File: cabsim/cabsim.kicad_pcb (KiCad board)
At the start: 2 copper layers, 87 x 30 mm, 45 parts, among them J1 NJ3FD-V, J3 Conn_01x01, J4 Conn_01x01, J5 NJ3FD-V, U3 Op_Amp_Dual, U4 Opamp_Quad

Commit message: update pcb
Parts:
- C4: value 1n -> 3.3n
- C7: value 2.2n -> 3.3n
- R19: value 390 -> 330
- R5, R9: value 3.9k -> 3.3k
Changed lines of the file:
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@@
 			)
 		)
-		(property "Value" "390"
+		(property "Value" "330"
 			(at 3.81 2.31 90)
 			(layer "F.Fab")
@@
 			)
 		)
-		(property "Value" "3.9k"
+		(property "Value" "3.3k"
 			(at 3.81 2.31 90)
 			(layer "F.Fab")
@@
 			)
 		)
-		(property "Value" "3.9k"
+		(property "Value" "3.3k"
 			(at 3.81 2.31 90)
 			(layer "F.Fab")
@@
 			)
 		)
-		(property "Value" "2.2n"
+		(property "Value" "3.3n"
 			(at 2.5 -2.31 90)
 			(layer "B.Fab")
@@
 			)
 		)
-		(property "Value" "1n"
+		(property "Value" "3.3n"
 			(at 2.5 -2.31 90)
 			(layer "B.Fab")

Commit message: update pcb and gitignore
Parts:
- C10, C12, C2, C9: moved to F.Cu
- moved R1 29.2 mm to (111.5, 83.3), turned to 180 degrees
- moved C2 27.3 mm to (108.7, 88.6)
- moved R17 27.0 mm to (152.5, 97.7), turned to 0 degrees
- moved R19 26.3 mm to (141.1, 81.4), turned to 0 degrees
- moved R5 20.8 mm to (115.8, 94.7)
- moved C12 19.2 mm to (115.7, 97.4)
- moved J3 19.0 mm to (98.8, 72.1)
- moved J4 18.6 mm to (116.2, 72.0)
- moved C14 18.4 mm to (147.0, 84.8), turned to 0 degrees
- moved R8 17.4 mm to (133.2, 94.9)
- moved R9 17.4 mm to (136.4, 87.2)
- moved C6 17.1 mm to (133.3, 97.5)
- moved C13 16.4 mm to (141.6, 84.8)
- moved R6 14.2 mm to (119.2, 87.0)
- moved C15 13.3 mm to (164.5, 87.7), turned to -90 degrees
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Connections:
- C2 pad 1: Net-(U4A-+) -> Net-(U4D-+)
- C4 pad 2: Net-(U4A--) -> Net-(U4D--)
- C5 pad 1: Net-(U4D-+) -> Net-(U4A-+)
- C7 pad 2: Net-(U4D--) -> Net-(U4A--)
- R1 pad 1: Net-(U4A-+) -> Net-(U4D-+)
- R5 pad 2: Net-(U4A--) -> Net-(U4D--)
- R6 pad 1: Net-(U4A--) -> Net-(U4D--)
- R8 pad 2: Net-(U4D-+) -> Net-(U4A-+)
- R9 pad 1: Net-(U4D--) -> Net-(U4A--)
- RV1 pad 1: Net-(U4D--) -> Net-(U4A--)
- RV1 pad 2: Net-(U4D--) -> Net-(U4A--)
- U4 pad 1: Net-(C4-Pad1) -> Net-(C7-Pad1)
- U4 pad 14: Net-(C7-Pad1) -> Net-(C4-Pad1)
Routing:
- net Net-(U4A--): track 10.4 -> 52.1 mm
- net Net-(U4D--): track 48.0 -> 9.47 mm
- net Net-(C2-Pad2): track 27.3 -> 5.31 mm
- net Net-(C15-Pad2): track 15.4 -> 37.1 mm
- net Net-(C10-Pad1): track 51.9 -> 64.2 mm
- net Net-(U3A-+): track 23.7 -> 35.6 mm
- net Net-(U3B-+): track 17.5 -> 7.97 mm
- net GND: track 14.5 -> 5.25 mm
- net /vref: track 110.4 -> 101.2 mm
- net Net-(U4D-+): track 9.69 -> 18.7 mm
- net Net-(U3C-V+): track 76.3 -> 84.4 mm
- net Net-(C13-Pad1): track 25.2 -> 17.1 mm
- net Net-(C7-Pad1): track 9.52 -> 16.9 mm
- net Net-(D1-A): track 20.1 -> 12.8 mm
- net Net-(U4A-+): track 12.5 -> 6.39 mm
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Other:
- outline, holes or cut-outs redrawn

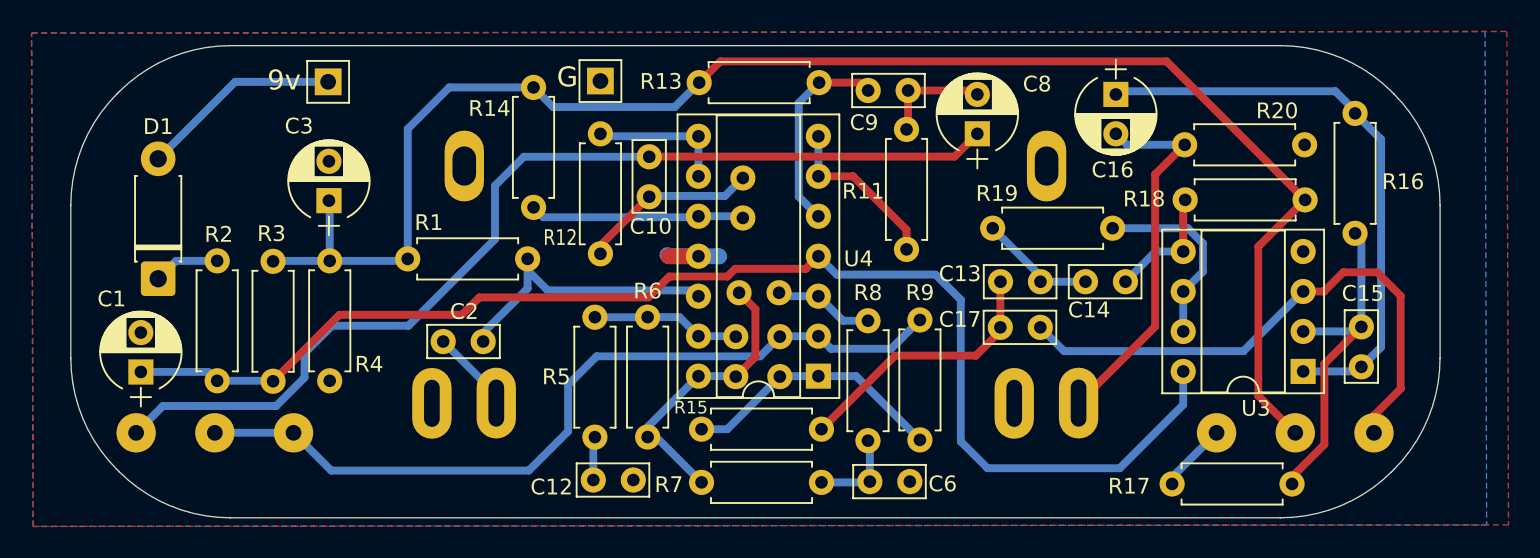
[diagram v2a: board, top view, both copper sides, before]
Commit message: minor routing adjustments
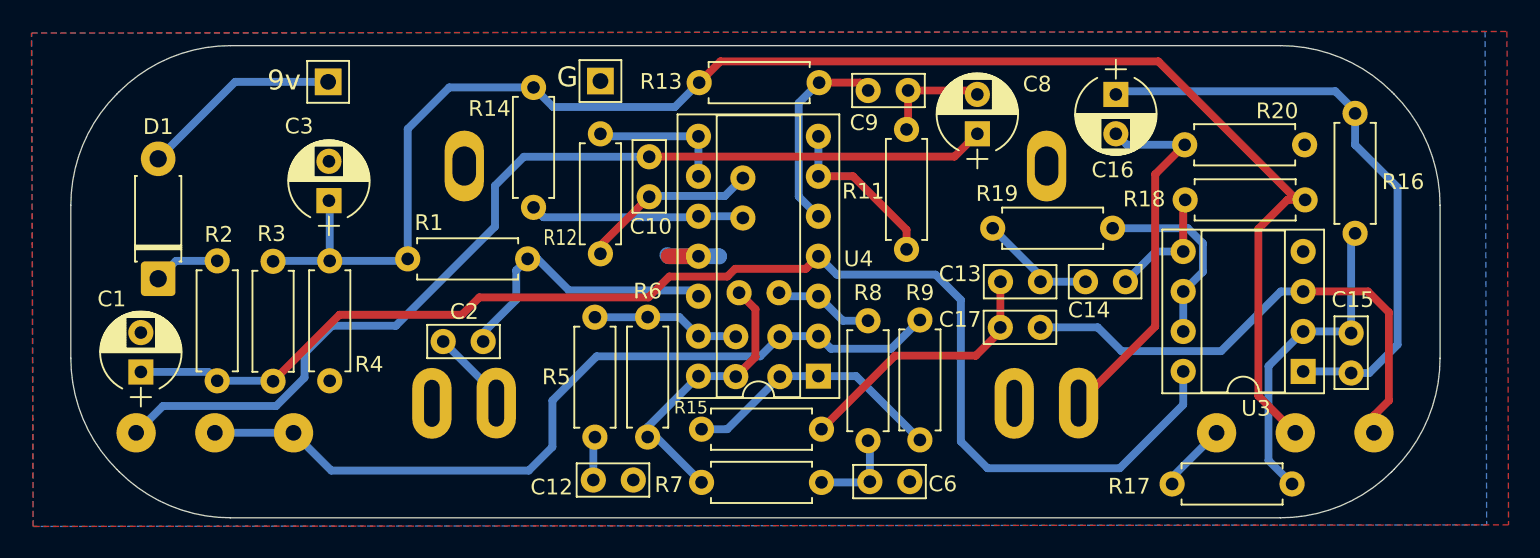
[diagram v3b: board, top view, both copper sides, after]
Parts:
- moved C15 0.76 mm to (163.8, 88.1)
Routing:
- net Net-(U3A-+): track 35.6 -> 32.9 mm
- net Net-(C15-Pad2): track 37.1 -> 38.6 mm
- net Net-(U3A--): track 21.7 -> 20.8 mm
- net /vref: track 101.2 -> 101.9 mm
